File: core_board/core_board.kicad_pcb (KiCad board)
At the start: 2 copper layers, 27 x 60 mm, 36 parts, among them J1 Conn_01x13_Socket, J2 Conn_01x13_Socket, J3 Ignitor Output, J4 Micro_SD_Card, J5 Battery Input, J7 Connector 1, J8 Connector 2, U1 CPC1002N, U2 CPC1002N, U3 CPC1002N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

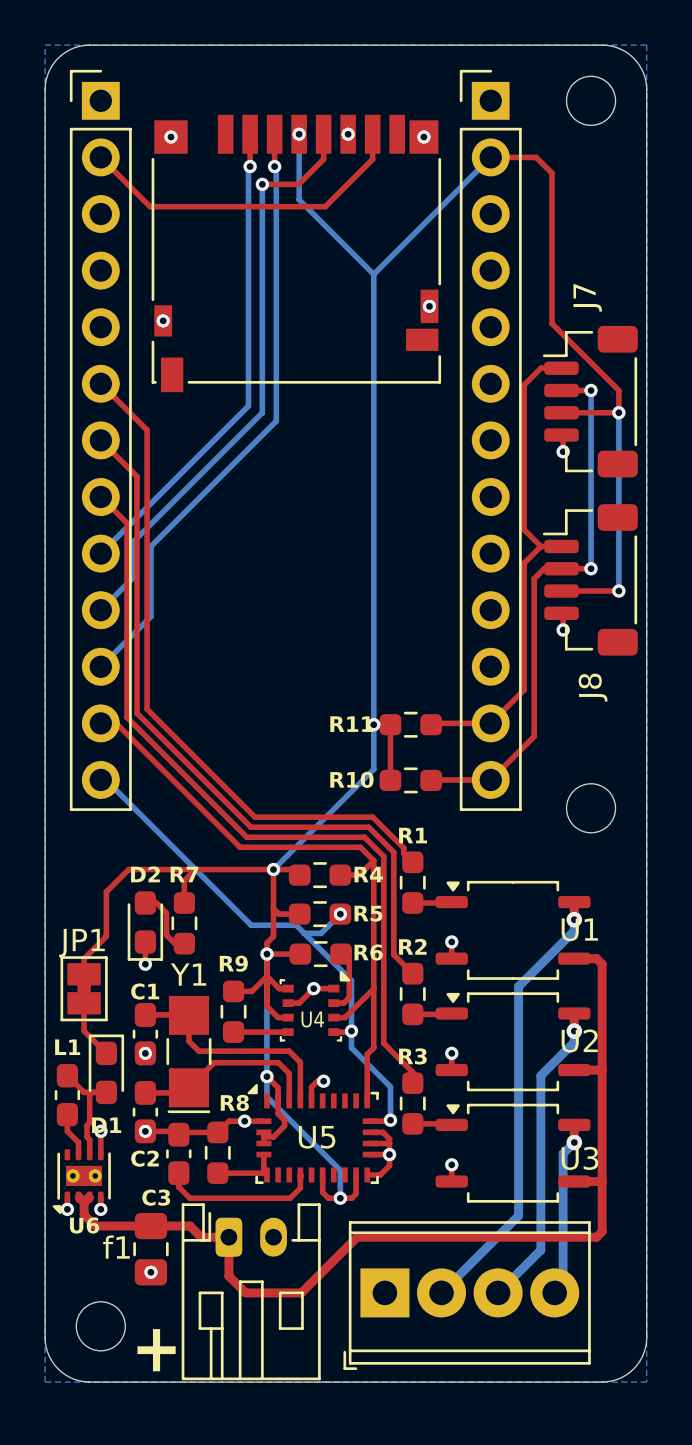
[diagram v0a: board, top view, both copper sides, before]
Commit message: Added Aerospace Club logo and gave mounting holes pads
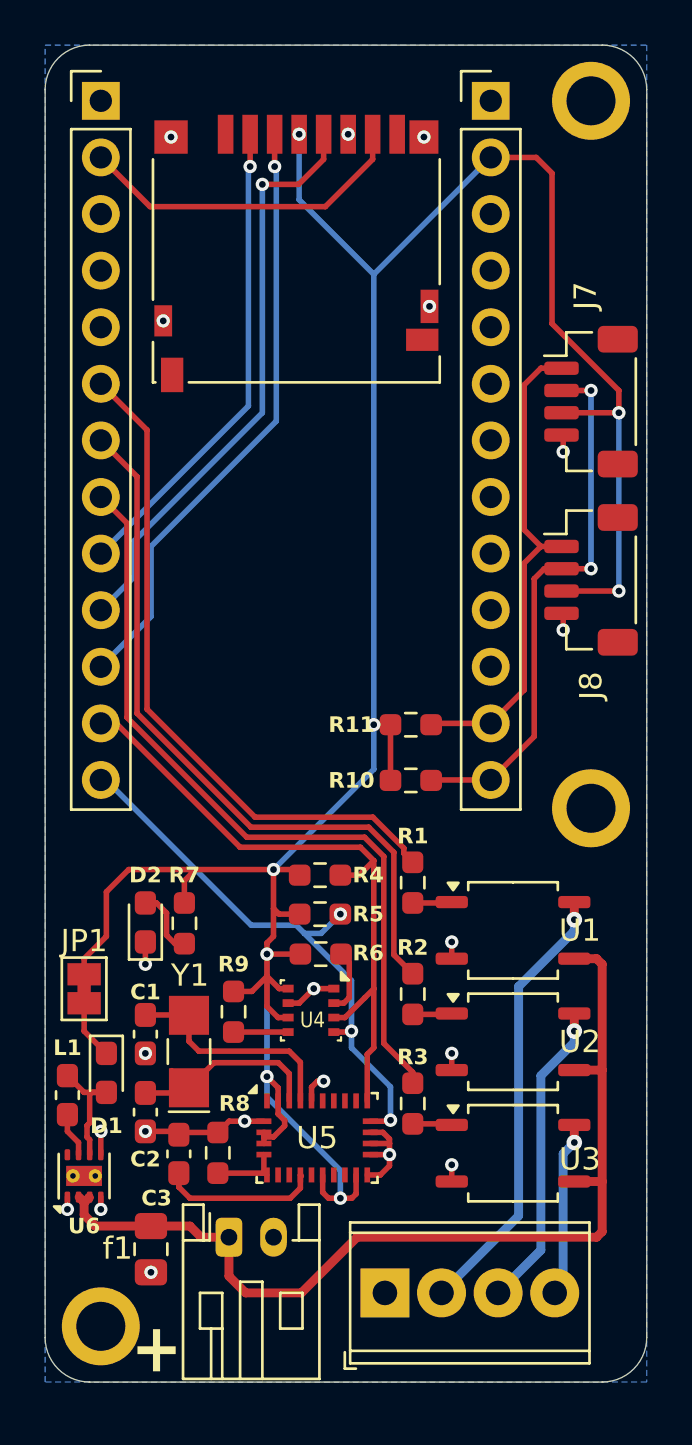
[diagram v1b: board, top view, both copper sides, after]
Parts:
- added G***: LOGO, LOGO, B.Cu at (111.0, 103.2)
- H1, H2, H3: footprint MountingHole:MountingHole_2.2mm_M2_ISO7380 -> MountingHole:MountingHole_2.2mm_M2_ISO7380_Pad
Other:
- board text added: "UNL Aerospace"
